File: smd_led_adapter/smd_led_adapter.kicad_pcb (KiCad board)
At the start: 2 copper layers, 15.2 x 20.3 mm, 14 parts, among them J1 Conn_01x08_Male, J2 Conn_01x08_Male

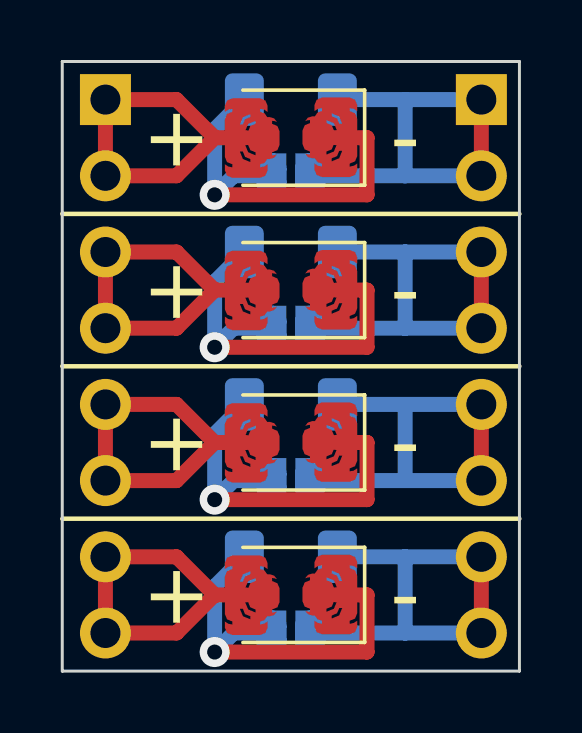
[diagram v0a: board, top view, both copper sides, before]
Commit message: Make smd led adaptor cathode/anode commonable.
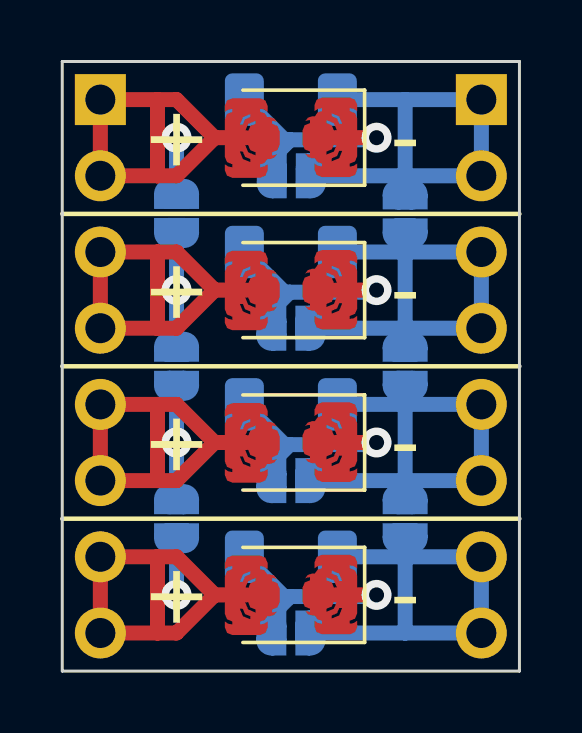
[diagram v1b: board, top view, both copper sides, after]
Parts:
- added JP10: SolderJumper_2_Open, Custom:SolderJumper-2_P1.3mm_Open_RoundedPad1.0x1.5mm, B.Cu at (174.0, 88.9)
- added JP5: SolderJumper_2_Open, Custom:SolderJumper-2_P1.3mm_Open_RoundedPad1.0x1.5mm, B.Cu at (170.2, 82.5)
- added JP6: SolderJumper_2_Open, Custom:SolderJumper-2_P1.3mm_Open_RoundedPad1.0x1.5mm, B.Cu at (170.2, 87.6)
- added JP7: SolderJumper_2_Open, Custom:SolderJumper-2_P1.3mm_Open_RoundedPad1.0x1.5mm, B.Cu at (170.2, 92.7)
- added JP8: SolderJumper_2_Open, Custom:SolderJumper-2_P1.3mm_Open_RoundedPad1.0x1.5mm, B.Cu at (174.0, 78.7)
- added JP9: SolderJumper_2_Open, Custom:SolderJumper-2_P1.3mm_Open_RoundedPad1.0x1.5mm, B.Cu at (174.0, 83.8)
- JP1, JP2, JP3, JP4: footprint Jumper:SolderJumper-2_P1.3mm_Open_RoundedPad1.0x1.5mm -> Custom:SolderJumper-2_P1.3mm_Open_RoundedPad1.0x1.5mm
- moved JP4 15.2 mm to (170.2, 77.5)
- moved JP3 4.02 mm to (166.4, 88.9), turned to -90 degrees
- moved JP2 4.02 mm to (166.4, 83.8), turned to -90 degrees
- moved JP1 4.01 mm to (166.4, 78.7), turned to -90 degrees
- moved J1 0.17 mm to (163.8, 74.9)
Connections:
- D1 pad 2: /VCC -> /VCC0
- D2 pad 2: /VCC -> /VCC1
- D3 pad 2: /VCC -> /VCC2
- D4 pad 2: /VCC -> /VCC3
- J1 pad 1: /VCC -> /VCC0
- J1 pad 2: /VCC -> /VCC0
- J1 pad 3: /VCC -> /VCC1
- J1 pad 4: /VCC -> /VCC1
- J1 pad 5: /VCC -> /VCC2
- J1 pad 6: /VCC -> /VCC2
- J1 pad 7: /VCC -> /VCC3
- J1 pad 8: /VCC -> /VCC3
- J2 pad 1: /GND -> /GND0
- J2 pad 2: /GND -> /GND0
- J2 pad 3: /GND -> /GND1
- J2 pad 4: /GND -> /GND1
- J2 pad 5: /GND -> /GND2
- J2 pad 6: /GND -> /GND2
- J2 pad 7: /GND -> /GND3
- J2 pad 8: /GND -> /GND3
- JP1 pad 1: Net-(D1-Pad1) -> /VCC0
- JP1 pad 2: /GND -> /VCC1
- JP2 pad 1: Net-(D2-Pad1) -> /VCC1
- JP2 pad 2: /GND -> /VCC2
- JP3 pad 1: Net-(D3-Pad1) -> /VCC2
- JP3 pad 2: /GND -> /VCC3
- JP4 pad 1: Net-(D4-Pad1) -> Net-(D1-Pad1)
- JP4 pad 2: /GND -> /GND0
- R1 pad 2: /GND -> /GND0
- R2 pad 2: /GND -> /GND1
- R3 pad 2: /GND -> /GND2
- R4 pad 2: /GND -> /GND3
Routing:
- net /GND: track 62.0 -> 0.00 mm
- net /VCC: track 47.7 -> 0.00 mm
- net /VCC1: track 0.00 -> 19.2 mm, vias 0 -> 1
- net /VCC2: track 0.00 -> 19.2 mm, vias 0 -> 1
- net /VCC3: track 0.00 -> 17.3 mm, vias 0 -> 1
- net /VCC0: track 0.00 -> 17.3 mm, vias 0 -> 1
- net /GND2: track 0.00 -> 16.8 mm
- net /GND1: track 0.00 -> 16.7 mm
- net /GND3: track 0.00 -> 16.1 mm
- net /GND0: track 0.00 -> 16.1 mm
- net Net-(D2-Pad1): track 13.7 -> 7.80 mm
- net Net-(D1-Pad1): track 13.7 -> 7.80 mm
- net Net-(D3-Pad1): track 13.7 -> 7.80 mm
- net Net-(D4-Pad1): track 13.7 -> 7.81 mm
- removed copper zone on B.Cu, net /GND
- removed copper zone on F.Cu, net /VCC
